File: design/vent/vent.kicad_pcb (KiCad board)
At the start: 2 copper layers, 81 parts, among them J1 A-DF 15 A/KG-T2S, J11 SD_Card_modified, J14 OSTYK21106030, J2 OSTYK22102030, Q1 DMG2302UK, Q2 DMG2302UK, Q3 AOD417, Q4 AOD417, Q5 DMG2302UK, Q6 DMG2302UK, Q7 AOD476, Q8 AOD476, U1 R-78E3.3-0.5, U10 MS5607-02BA03, U11 SPU01M-15, U2 SN74LVC2T45, U3 XBEE_SC1, U4 SN74LVC2T45, U5 SN74LVC2T45, U6 LP2980AIM5-3.0, U7 LSM6DS3HTR, U8 BMG250, U9 LSM6DS3HTR

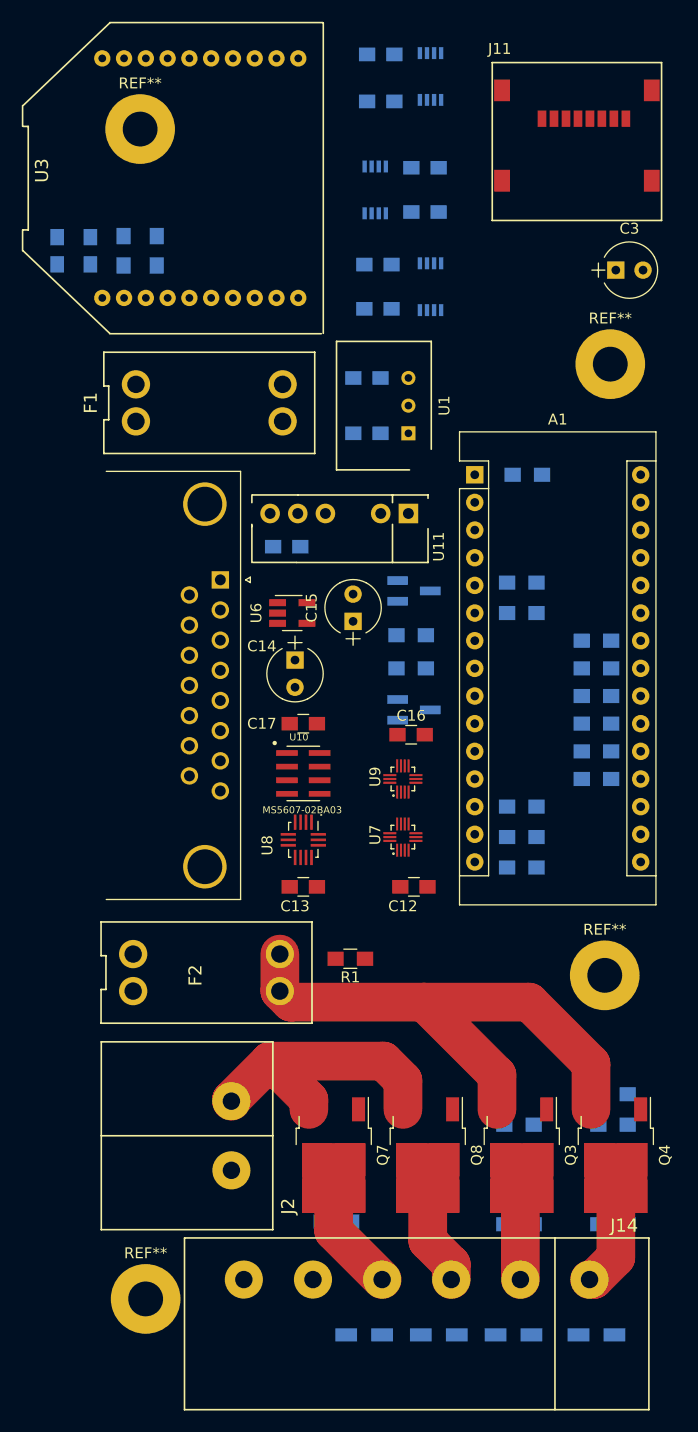
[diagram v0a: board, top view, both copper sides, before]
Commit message: Final vent/injector layout + routing
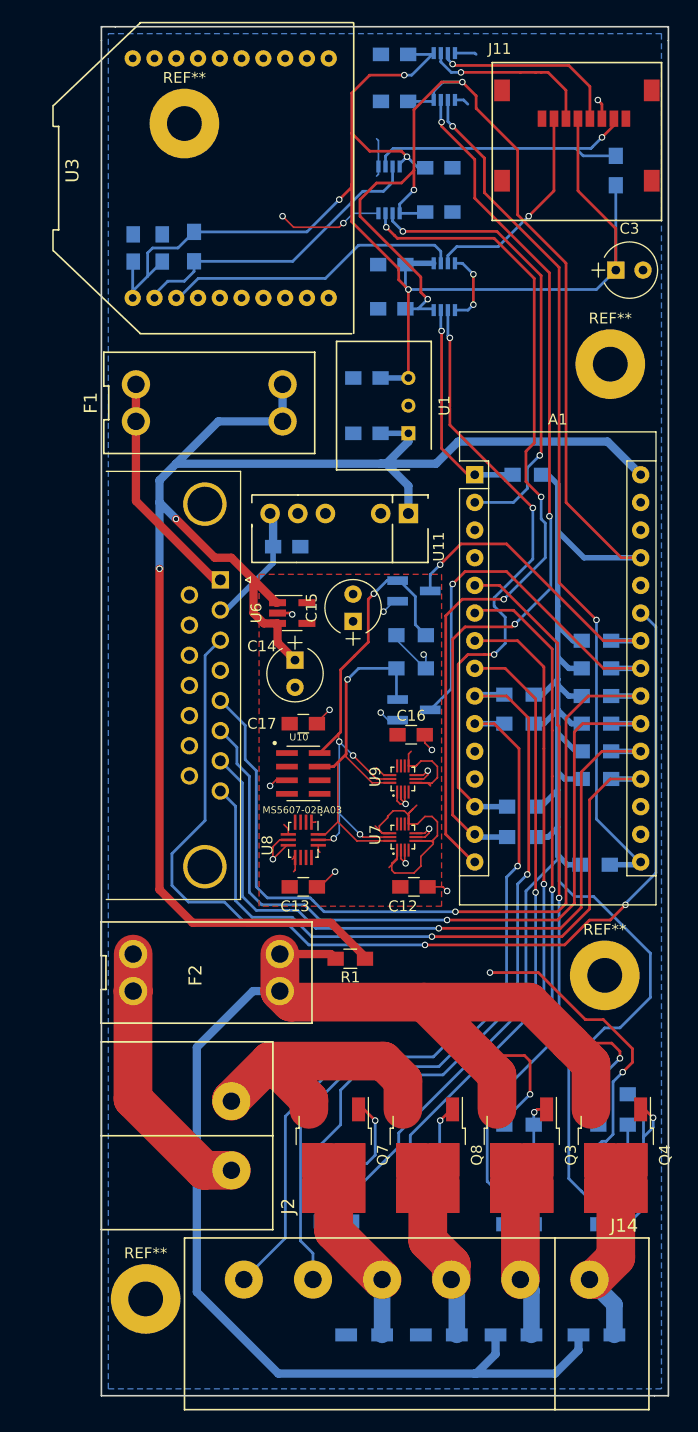
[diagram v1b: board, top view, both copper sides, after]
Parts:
- moved R12 42.8 mm to (131.3, 52.3), turned to 90 degrees
- moved R15 10.3 mm to (122.4, 100.5)
- moved R16 10.2 mm to (122.4, 103.1)
- moved C7 6.99 mm to (87.0, 59.4), turned to 90 degrees
- moved R8 6.74 mm to (129.4, 116.1), turned to 0 degrees
- moved C6 6.61 mm to (89.7, 59.4), turned to 90 degrees
- moved R11 6.49 mm to (92.6, 59.3)
- moved REF** 4.10 mm to (91.7, 48.0)
- moved U3 2.79 mm to (90.4, 51.8)
- moved C4 1.27 mm to (111.0, 46.0)
- moved C5 1.27 mm to (111.0, 41.7)
- moved C10 1.27 mm to (115.1, 56.1)
- moved C11 1.27 mm to (115.1, 52.1)
- moved C8 1.27 mm to (110.7, 65.0)
- moved C9 1.27 mm to (110.7, 61.0)
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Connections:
- A1 pad 10: /Valve Control/LOW_SIDE_B -> /Valve Control/LIM_CLOSE
- A1 pad 5: /Valve Control/LIM_CLOSE -> /Valve Control/HIGH_SIDE_B
- A1 pad 6: /Valve Control/LIM_OPEN -> /Valve Control/HIGH_SIDE_A
- A1 pad 7: /Valve Control/HIGH_SIDE_A -> /Valve Control/LOW_SIDE_B
- A1 pad 9: /Valve Control/HIGH_SIDE_B -> /Valve Control/LIM_OPEN
- J1 pad 10: /Sensors Analog/THERM_3 -> CTL_POWER_GND
- J1 pad 12: /Sensors Analog/THERM_4 -> CTL_POWER_GND
- J1 pad 14: SDA_5V -> CTL_POWER_GND
- J1 pad 15: SCL_5V -> CTL_POWER_GND
- J1 pad 2: CTL_POWER_GND -> +15V
- J1 pad 3: +15V -> /Sensors Analog/PRESSURE
- J1 pad 4: /Sensors Analog/PRESSURE -> CTL_POWER_GND
- J1 pad 5: CTL_POWER_GND -> /Sensors Analog/THERM_4
- J1 pad 6: /Sensors Analog/THERM_1 -> /Sensors Analog/THERM_3
- J1 pad 7: CTL_POWER_GND -> /Sensors Analog/THERM_2
- J1 pad 8: /Sensors Analog/THERM_2 -> /Sensors Analog/THERM_1
- U2 pad 2: /Comms & Logging/MISO_3V3 -> /Comms & Logging/MOSI_3V3
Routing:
- net +5V: track 0.00 -> 246.8 mm, vias 0 -> 3
- net +11.1V: track 0.00 -> 157.4 mm, vias 0 -> 2
- net +3V3: track 0.00 -> 131.4 mm, vias 0 -> 4
- net VALVE_POWER: track 51.5 -> 155.7 mm, vias 0 -> 2
- net /Sensors Analog/PRESSURE: track 0.00 -> 98.4 mm, vias 0 -> 2
- net CTL_POWER_GND: track 26.7 -> 110.9 mm, vias 0 -> 18
- net /Comms & Logging/MOSI_5V: track 0.00 -> 82.0 mm, vias 0 -> 3
- net /Comms & Logging/SCK_5V: track 0.00 -> 80.3 mm, vias 0 -> 2
- net /Comms & Logging/MISO_5V: track 0.00 -> 78.7 mm, vias 0 -> 3
- net /Sensors Analog/THERM_4: track 0.00 -> 75.6 mm, vias 0 -> 1
- net /Valve Control/LIM_OPEN: track 0.00 -> 74.0 mm, vias 0 -> 1
- net /Sensors Analog/THERM_3: track 0.00 -> 72.4 mm, vias 0 -> 1
- net /Valve Control/LIM_CLOSE: track 0.00 -> 71.7 mm, vias 0 -> 1
- net /Sensors Analog/THERM_2: track 0.00 -> 67.8 mm, vias 0 -> 1
- net /Sensors Analog/THERM_1: track 0.00 -> 63.8 mm, vias 0 -> 1
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- added copper zone on F.Cu, net +3.0V
- added copper zone on B.Cu, net CTL_POWER_GND
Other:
- board outline added: 52.1 x 125.7 mm
- net class Default: clearance 0.2 -> 0.127; trace_width 0.25 -> 0.127
- rule pad_to_mask_clearance: 0.2 -> 0.0508
- rule trace_clearance: 0.2 -> 0.127
- rule trace_min: 0.2 -> 0.127

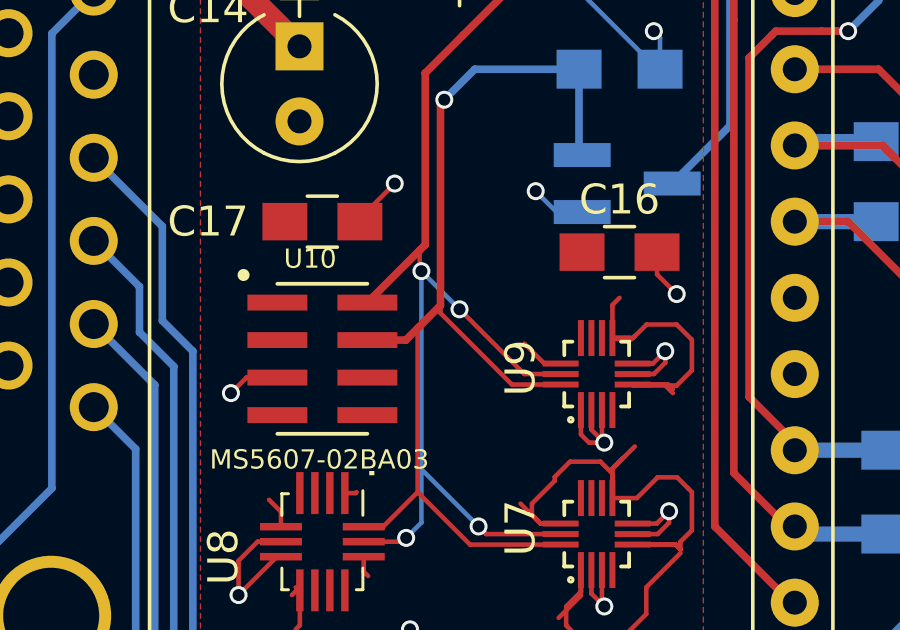
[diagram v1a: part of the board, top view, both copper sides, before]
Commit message: Tweak 3V pour, regenerate gerbers
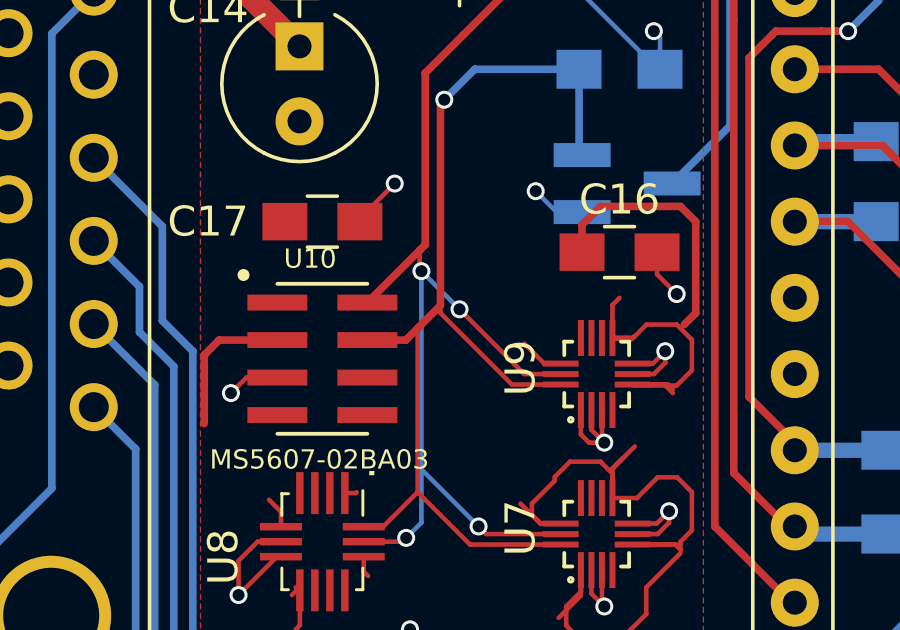
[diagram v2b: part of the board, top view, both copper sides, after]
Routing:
- net +3.0V: track 54.6 -> 68.2 mm
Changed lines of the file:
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@@
     (thickness 1.6)
     (drawings 10)
-    (tracks 858)
+    (tracks 867)
     (zones 0)
     (modules 81)
@@
     (visible_elements FFFEFF7F)
     (pcbplotparams
-      (layerselection 0x000f0_80000001)
-      (usegerberextensions false)
+      (layerselection 0x010f0_80000001)
+      (usegerberextensions true)
       (excludeedgelayer true)
       (linewidth 0.100000)
       (plotframeref false)
-      (viasonmask false)
+      (viasonmask true)
       (mode 1)
       (useauxorigin false)
@@
       (drillshape 0)
       (scaleselection 1)
-      (outputdirectory ""))
+      (outputdirectory ../../fab/vent/gerbers/))
   )
   (net 0 "")
@@
   (segment (start 86.9485 63.3995) (end 88.3185 62.0295) (width 0.254) (layer B.Cu) (net 30))
   (segment (start 88.3185 62.0295) (end 89.662 60.686) (width 0.254) (layer B.Cu) (net 30))
+  (segment (start 111.272 104.14) (end 111.272 103.231) (width 0.254) (layer F.Cu) (net 31) (status 400000))
+  (segment (start 115.062 106.172) (end 114.681 106.553) (width 0.254) (layer F.Cu) (net 31))
+  (segment (start 115.062 103.124) (end 115.062 106.172) (width 0.254) (layer F.Cu) (net 31))
+  (segment (start 114.554 102.616) (end 115.062 103.124) (width 0.254) (layer F.Cu) (net 31))
+  (segment (start 111.887 102.616) (end 114.554 102.616) (width 0.254) (layer F.Cu) (net 31))
+  (segment (start 111.272 103.231) (end 111.887 102.616) (width 0.254) (layer F.Cu) (net 31))
+  (segment (start 101.116 107.071) (end 99.177 107.071) (width 0.254) (layer F.Cu) (net 31) (status 400000))
+  (segment (start 98.679 107.569) (end 98.679 109.855) (width 0.254) (layer F.Cu) (net 31))
+  (segment (start 99.177 107.071) (end 98.679 107.569) (width 0.254) (layer F.Cu) (net 31))
   (segment (start 111.235 114.738) (end 111.235 115.46) (width 0.1524) (layer F.Cu) (net 31))
   (segment (start 113.411 115.316) (end 114.554 114.173) (width 0.1524) (layer F.Cu) (net 31))

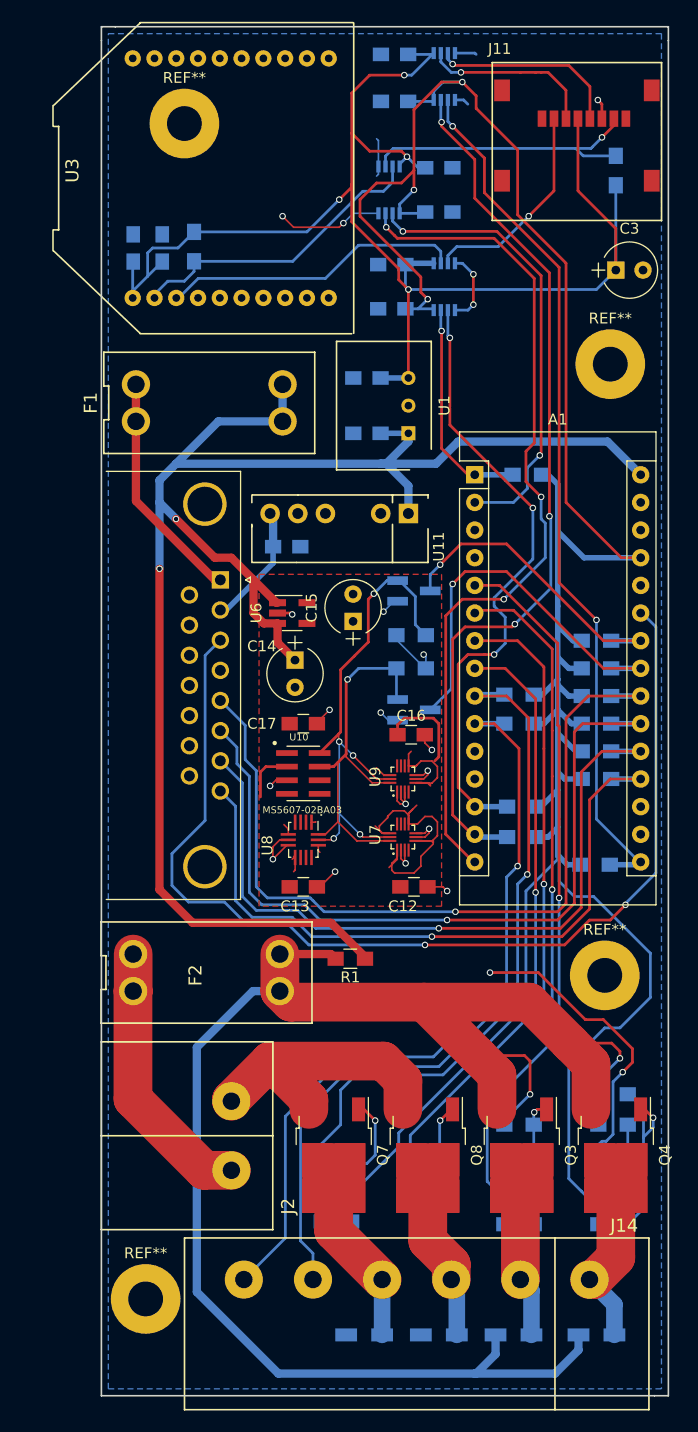
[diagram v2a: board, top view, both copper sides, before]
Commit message: Update silkscreen, regen gerbers
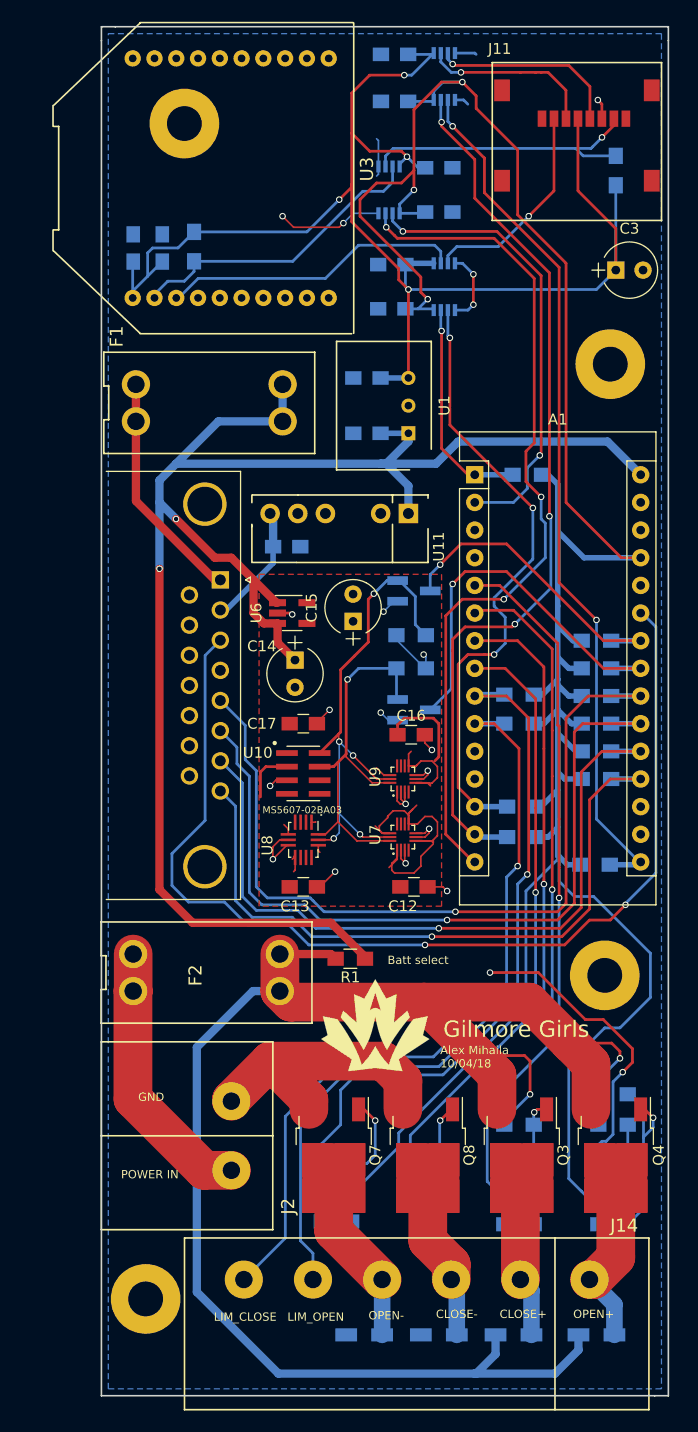
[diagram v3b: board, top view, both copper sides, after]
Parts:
- added G***: LOGO, Team_Logo:Logo_SilkScreen_10mm, F.Cu at (109.2, 130.8)
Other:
- board text added: "Alex Mihaila 10/04/18"
- board text added: "Batt select"
- board text added: "CLOSE+"
- board text added: "CLOSE-"
- board text added: "GND"
- board text added: "Gilmore Girls"
- board text added: "LIM_CLOSE"
- board text added: "LIM_OPEN"
- board text added: "OPEN+"
- board text added: "OPEN-"
- board text added: "POWER IN"
